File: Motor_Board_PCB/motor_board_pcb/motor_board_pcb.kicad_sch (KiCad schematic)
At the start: 13 parts, among them U1 MCP2515-xST, U2 TJA1050, Y1 20M

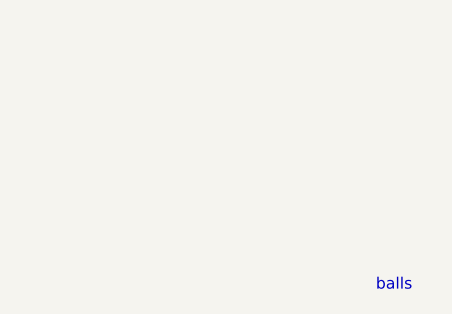
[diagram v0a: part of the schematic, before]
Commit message: removed balls
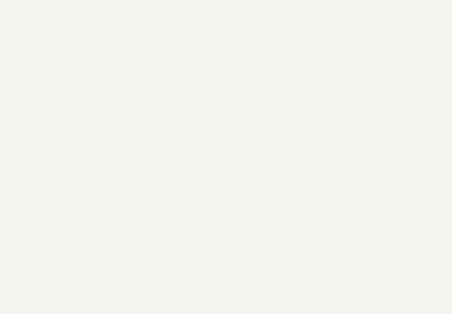
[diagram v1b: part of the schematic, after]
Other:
- note removed: "balls"
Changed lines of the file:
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@@
-    (effects (font (size 1.27 1.27)) (justify left bottom))
-  )
-  (text "balls" (at 184.15 176.53 0)
     (effects (font (size 1.27 1.27)) (justify left bottom))
   )

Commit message: added balls
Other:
- note added: "balls"
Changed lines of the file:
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@@
+    (effects (font (size 1.27 1.27)) (justify left bottom))
+  )
+  (text "balls" (at 184.15 176.53 0)
     (effects (font (size 1.27 1.27)) (justify left bottom))
   )
